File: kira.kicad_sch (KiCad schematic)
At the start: 34 parts, among them J1 USB_C_Receptacle_USB2.0, J2 SWD, SW46 Boot, SW47 Reset, U1 RP2040, U2 XC6206PxxxMR, U3 W25Q128JVS, U4 USBLC6-2SC6, Y1 12MHz

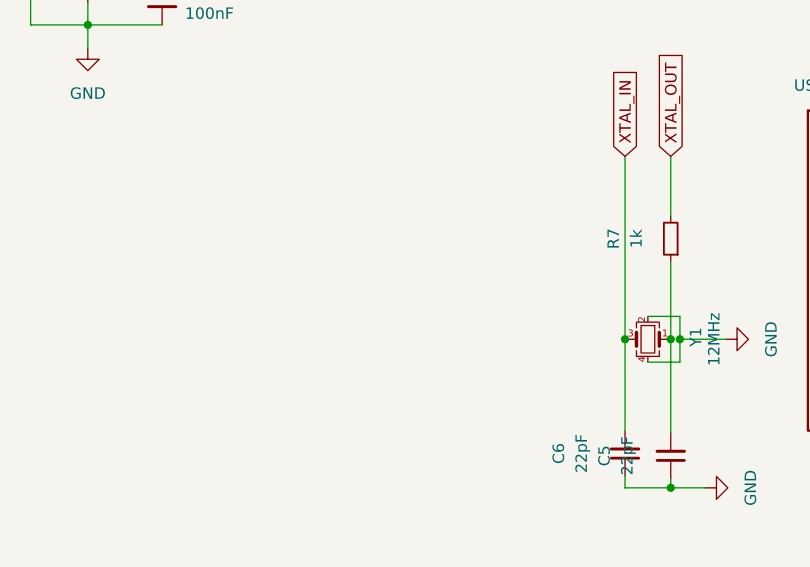
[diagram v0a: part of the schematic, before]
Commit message: added JST port, updated production files
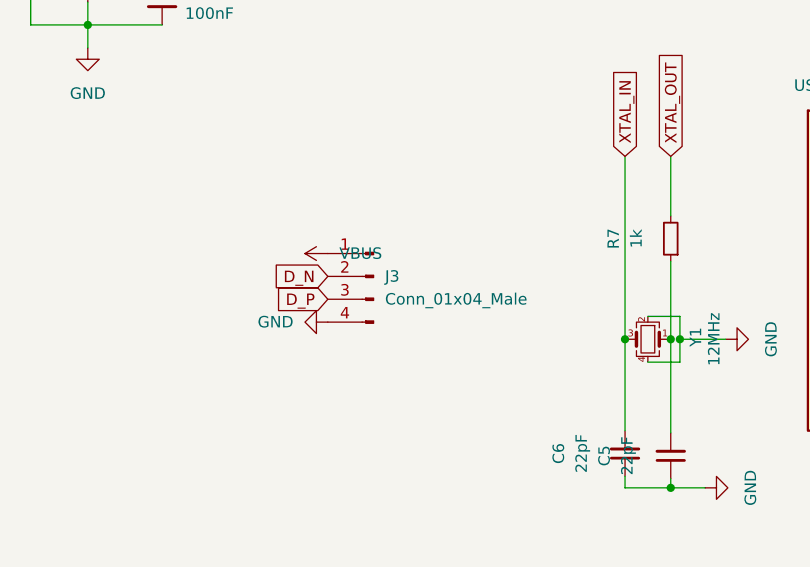
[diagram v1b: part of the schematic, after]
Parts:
- added J3: Conn_01x04_Male, random-keyboard-parts:JST-SR-4, symbol Connector:Conn_01x04_Male
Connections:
- net D_N: now also J3.2 (Pin_2)
- net D_P: now also J3.3 (Pin_3)
- net GND: now also J3.4 (Pin_4)
- net VBUS: now also J3.1 (Pin_1)
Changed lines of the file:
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@@
+    )
+  )
+  (global_label "D_N" (shape input) (at 154.305 92.71 180) (fields_autoplaced)
+    (effects (font (size 1.27 1.27)) (justify right))
+    (property "Intersheet References" "${INTERSHEET_REFS}" (id 0) (at 148.3238 92.6306 0)
+      (effects (font (size 1.27 1.27)) (justify right) hide)
     )
   )
@@
     (property "Intersheet References" "${INTERSHEET_REFS}" (id 0) (at 77.1919 53.8956 0)
       (effects (font (size 1.27 1.27)) (justify left) hide)
+    )
+  )
+  (global_label "D_P" (shape input) (at 154.305 95.25 180) (fields_autoplaced)
+    (effects (font (size 1.27 1.27)) (justify right))
+    (property "Intersheet References" "${INTERSHEET_REFS}" (id 0) (at 148.3843 95.1706 0)
+      (effects (font (size 1.27 1.27)) (justify right) hide)
     )
   )
@@
     (pin "2")
   )
+  (symbol (lib_name "GND_1") (lib_id "power:GND") (at 154.305 97.79 270) (unit 1)
+    (in_bom yes) (on_board yes) (fields_autoplaced)
+    (property "Reference" "#PWR0132" (id 0) (at 147.955 97.79 0)
+      (effects (font (size 1.27 1.27)) hide)
+    )
+    (property "Value" "GND" (id 1) (at 150.495 97.7899 90)
+      (effects (font (size 1.27 1.27)) (justify right))
+    )
+    (property "Footprint" "" (id 2) (at 154.305 97.79 0)
+      (effects (font (size 1.27 1.27)) hide)
+    )
+    (property "Datasheet" "" (id 3) (at 154.305 97.79 0)
+      (effects (font (size 1.27 1.27)) hide)
+    )
+    (pin "1")
+  )
   (symbol (lib_id "power:+3V3") (at 27.305 69.215 0) (unit 1)
     (in_bom yes) (on_board yes) (fields_autoplaced)
@@
     )
     (property "Datasheet" "" (id 3) (at 198.501 99.695 0)
+      (effects (font (size 1.27 1.27)) hide)
+    )
+    (pin "1")
+  )
+  (symbol (lib_id "power:VBUS") (at 154.305 90.17 90) (unit 1)
+    (in_bom yes) (on_board yes) (fields_autoplaced)
+    (property "Reference" "#PWR0101" (id 0) (at 158.115 90.17 0)
+      (effects (font (size 1.27 1.27)) hide)
+    )
+    (property "Value" "VBUS" (id 1) (at 155.575 90.1699 90)
+      (effects (font (size 1.27 1.27)) (justify right))
+    )
+    (property "Footprint" "" (id 2) (at 154.305 90.17 0)
+      (effects (font (size 1.27 1.27)) hide)
+    )
+    (property "Datasheet" "" (id 3) (at 154.305 90.17 0)
       (effects (font (size 1.27 1.27)) hide)
     )
@@
     (pin "2")
   )
+  (symbol (lib_id "Connector:Conn_01x04_Male") (at 159.385 92.71 0) (mirror y) (unit 1)
+    (in_bom yes) (on_board yes) (fields_autoplaced)
+    (property "Reference" "J3" (id 0) (at 160.655 92.7099 0)
+      (effects (font (size 1.27 1.27)) (justify right))
+    )
+    (property "Value" "Conn_01x04_Male" (id 1) (at 160.655 95.2499 0)
+      (effects (font (size 1.27 1.27)) (justify right))
+    )
+    (property "Footprint" "random-keyboard-parts:JST-SR-4" (id 2) (at 159.385 92.71 0)
+      (effects (font (size 1.27 1.27)) hide)
+    )
+    (property "Datasheet" "~" (id 3) (at 159.385 92.71 0)
+      (effects (font (size 1.27 1.27)) hide)
+    )
+    (pin "1")
+    (pin "2")
+    (pin "3")
+    (pin "4")
+  )
   (symbol (lib_id "Device:C_Small") (at 163.449 31.115 0) (unit 1)
     (in_bom yes) (on_board yes)
@@
   )
   (symbol_instances
+    (path "/aee96a0d-47c5-4a17-bd1b-e9cf8b6431d7"
+      (reference "#PWR0101") (unit 1) (value "VBUS") (footprint "")
+    )
     (path "/ccd001ff-ffd1-45d5-a166-2f748b8f1ba2"
       (reference "#PWR0102") (unit 1) (value "GND") (footprint "")
@@
       (reference "#PWR0131") (unit 1) (value "GND") (footprint "")
     )
+    (path "/8b2be492-7af8-42ef-a1d8-ba0eb8496776"
+      (reference "#PWR0132") (unit 1) (value "GND") (footprint "")
+    )
     (path "/0ddedf06-cea5-4a1f-bea2-2a45031a82ea"
       (reference "C1") (unit 1) (value "1uF") (footprint "Capacitor_SMD:C_0402_1005Metric")
@@
       (reference "J2") (unit 1) (value "SWD") (footprint "Connector_PinSocket_2.54mm:PinSocket_1x05_P2.54mm_Vertical")
     )
+    (path "/f8d14650-cabb-4733-b815-574cdbb0222a"
+      (reference "J3") (unit 1) (value "Conn_01x04_Male") (footprint "random-keyboard-parts:JST-SR-4")
+    )
     (path "/251ac979-6893-4e2e-b711-4b1c15cd90f7"
